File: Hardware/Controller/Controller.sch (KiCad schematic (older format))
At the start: 6 parts

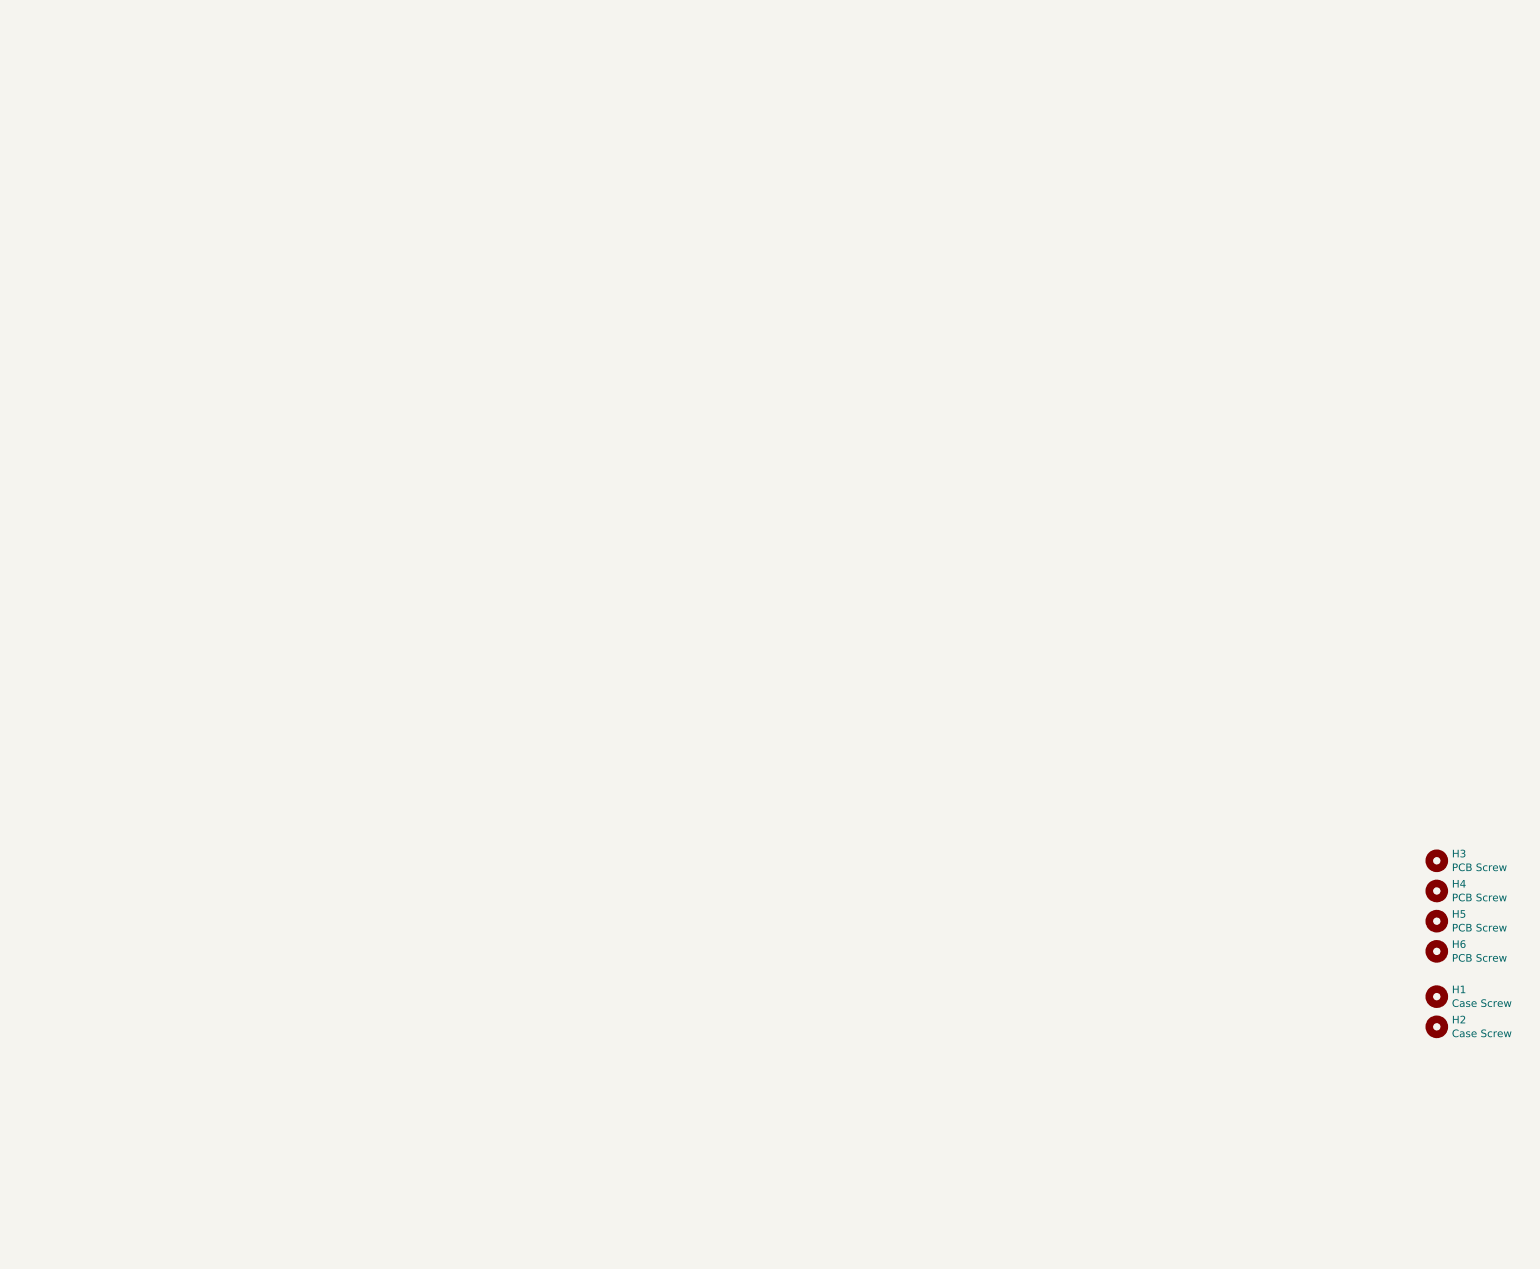
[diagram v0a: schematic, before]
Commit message: Updated fitting for SP 2090 enclosure
Better fit, but still not perfect.
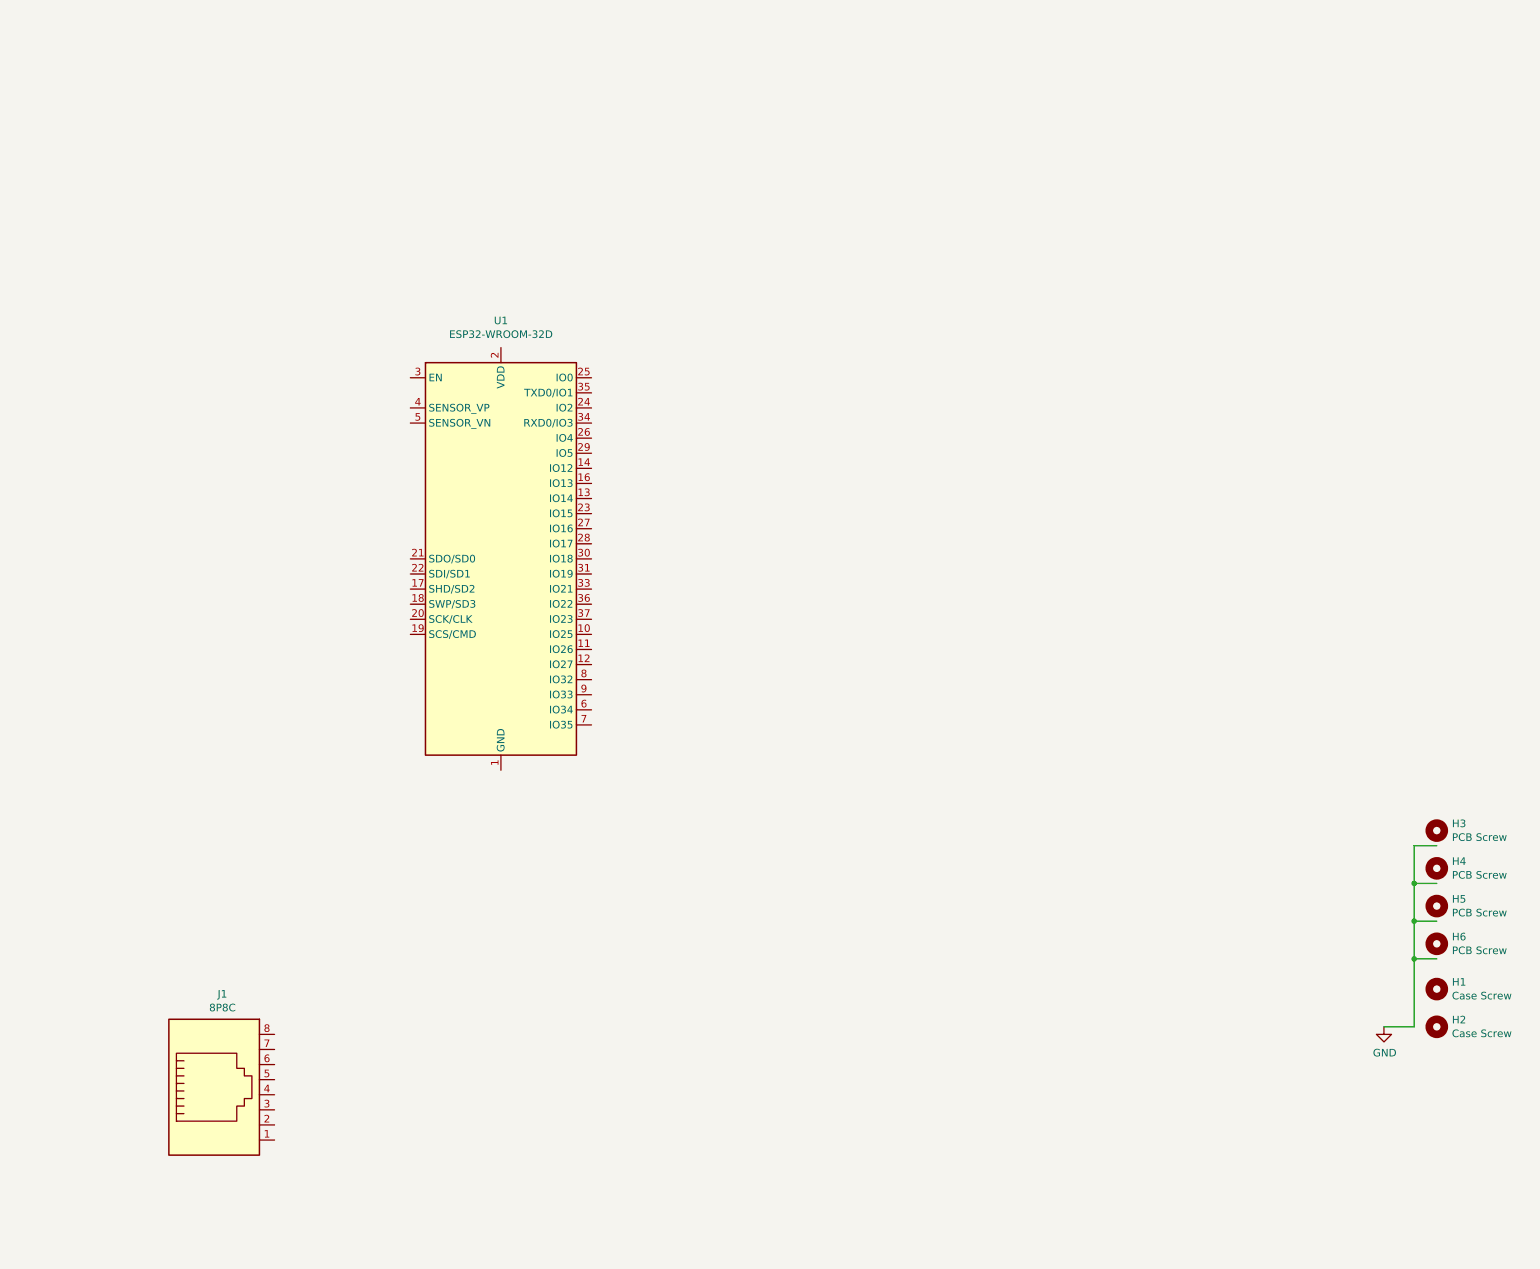
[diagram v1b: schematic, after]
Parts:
- added J1: 8P8C, Connector_RJ:RJ45_Amphenol_54602-x08_Horizontal, symbol Connector:8P8C
- added U1: ESP32-WROOM-32D, RF_Module:ESP32-WROOM-32, symbol RF_Module:ESP32-WROOM-32D
- H3, H4, H5, H6: footprint MountingHole:MountingHole_2.5mm -> MountingHole:MountingHole_2.7mm_M2.5
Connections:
- net labels added: GND
- wire segments 0 -> 9
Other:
- moved on the sheet: H1, H3, H4, H5, H6
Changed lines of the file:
@@
 EESchema Schematic File Version 4
+LIBS:Controller-cache
 EELAYER 26 0
 EELAYER END
@@
 L Mechanical:MountingHole H1
 U 1 1 5C67C5A6
-P 10000 6100
-F 0 "H1" H 10100 6146 50  0000 L CNN
-F 1 "Case Screw" H 10100 6055 50  0000 L CNN
-F 2 "MountingHole:MountingHole_5.3mm_M5" H 10000 6100 50  0001 C CNN
-F 3 "~" H 10000 6100 50  0001 C CNN
-	1    10000 6100
+P 10000 6050
+F 0 "H1" H 10100 6096 50  0000 L CNN
+F 1 "Case Screw" H 10100 6005 50  0000 L CNN
+F 2 "MountingHole:MountingHole_5.3mm_M5" H 10000 6050 50  0001 C CNN
+F 3 "~" H 10000 6050 50  0001 C CNN
+	1    10000 6050
 	1    0    0    -1
 $EndComp
@@
 L Mechanical:MountingHole H6
 U 1 1 5C67C6B3
-P 10000 5800
-F 0 "H6" H 10100 5846 50  0000 L CNN
-F 1 "PCB Screw" H 10100 5755 50  0000 L CNN
-F 2 "MountingHole:MountingHole_2.5mm" H 10000 5800 50  0001 C CNN
-F 3 "~" H 10000 5800 50  0001 C CNN
-	1    10000 5800
+P 10000 5750
+F 0 "H6" H 10100 5796 50  0000 L CNN
+F 1 "PCB Screw" H 10100 5705 50  0000 L CNN
+F 2 "MountingHole:MountingHole_2.7mm_M2.5" H 10000 5750 50  0001 C CNN
+F 3 "~" H 10000 5750 50  0001 C CNN
+	1    10000 5750
 	1    0    0    -1
 $EndComp
@@
 L Mechanical:MountingHole H5
 U 1 1 5C67C6E9
-P 10000 5600
-F 0 "H5" H 10100 5646 50  0000 L CNN
-F 1 "PCB Screw" H 10100 5555 50  0000 L CNN
-F 2 "MountingHole:MountingHole_2.5mm" H 10000 5600 50  0001 C CNN
-F 3 "~" H 10000 5600 50  0001 C CNN
-	1    10000 5600
+P 10000 5500
+F 0 "H5" H 10100 5546 50  0000 L CNN
+F 1 "PCB Screw" H 10100 5455 50  0000 L CNN
+F 2 "MountingHole:MountingHole_2.7mm_M2.5" H 10000 5500 50  0001 C CNN
+F 3 "~" H 10000 5500 50  0001 C CNN
+	1    10000 5500
 	1    0    0    -1
 $EndComp
@@
 L Mechanical:MountingHole H4
 U 1 1 5C67C721
-P 10000 5400
-F 0 "H4" H 10100 5446 50  0000 L CNN
-F 1 "PCB Screw" H 10100 5355 50  0000 L CNN
-F 2 "MountingHole:MountingHole_2.5mm" H 10000 5400 50  0001 C CNN
-F 3 "~" H 10000 5400 50  0001 C CNN
-	1    10000 5400
+P 10000 5250
+F 0 "H4" H 10100 5296 50  0000 L CNN
+F 1 "PCB Screw" H 10100 5205 50  0000 L CNN
+F 2 "MountingHole:MountingHole_2.7mm_M2.5" H 10000 5250 50  0001 C CNN
+F 3 "~" H 10000 5250 50  0001 C CNN
+	1    10000 5250
 	1    0    0    -1
 $EndComp
@@
 L Mechanical:MountingHole H3
 U 1 1 5C67C753
-P 10000 5200
-F 0 "H3" H 10100 5246 50  0000 L CNN
-F 1 "PCB Screw" H 10100 5155 50  0000 L CNN
-F 2 "MountingHole:MountingHole_2.5mm" H 10000 5200 50  0001 C CNN
-F 3 "~" H 10000 5200 50  0001 C CNN
-	1    10000 5200
+P 10000 5000
+F 0 "H3" H 10100 5046 50  0000 L CNN
+F 1 "PCB Screw" H 10100 4955 50  0000 L CNN
+F 2 "MountingHole:MountingHole_2.7mm_M2.5" H 10000 5000 50  0001 C CNN
+F 3 "~" H 10000 5000 50  0001 C CNN
+	1    10000 5000
 	1    0    0    -1
 $EndComp
+$Comp
+L power:GND #PWR0101
+U 1 1 5C688870
+P 9650 6300
+F 0 "#PWR0101" H 9650 6050 50  0001 C CNN
+F 1 "GND" H 9655 6127 50  0000 C CNN
+F 2 "" H 9650 6300 50  0001 C CNN
+F 3 "" H 9650 6300 50  0001 C CNN
+	1    9650 6300
+	1    0    0    -1
+$EndComp
+Wire Wire Line
+	10000 5100 9850 5100
+Wire Wire Line
+	9850 5100 9850 5350
+Wire Wire Line
+	9850 6300 9650 6300
+Wire Wire Line
+	10000 5850 9850 5850
+Connection ~ 9850 5850
+Wire Wire Line
+	10000 5600 9850 5600
+Connection ~ 9850 5600
+Wire Wire Line
+	9850 5600 9850 5850
+Wire Wire Line
+	10000 5350 9850 5350
+Connection ~ 9850 5350
+Wire Wire Line
+	9850 5350 9850 5600
+Wire Wire Line
+	9850 5850 9850 6300
+$Comp
+L RF_Module:ESP32-WROOM-32D U1
+U 1 1 5C688B86
+P 3800 3200
+F 0 "U1" H 3800 4778 50  0000 C CNN
+F 1 "ESP32-WROOM-32D" H 3800 4687 50  0000 C CNN
+F 2 "RF_Module:ESP32-WROOM-32" H 3800 1700 50  0001 C CNN
+F 3 "https://www.espressif.com/sites/default/files/documentation/esp32-wroom-32d_esp32-wroom-32u_datasheet_en.pdf" H 3500 3250 50  0001 C CNN
+	1    3800 3200
+	1    0    0    -1
+$EndComp
+$Comp
+L Connector:8P8C J1
+U 1 1 5C688D10
+P 1900 6750
+F 0 "J1" H 1955 7417 50  0000 C CNN
+F 1 "8P8C" H 1955 7326 50  0000 C CNN
+F 2 "Connector_RJ:RJ45_Amphenol_54602-x08_Horizontal" V 1900 6775 50  0001 C CNN
+F 3 "~" V 1900 6775 50  0001 C CNN
+	1    1900 6750
+	1    0    0    -1
+$EndComp

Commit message: Added a first set of parts
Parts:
- added J2: LCD Header, Connector_PinHeader_2.54mm:PinHeader_1x04_P2.54mm_Vertical, symbol Connector:Conn_01x04_Female
- added J3: USB_B_Micro, Connector_USB:USB_Micro-B_Amphenol_10103594-0001LF_Horizontal, symbol Connector:USB_B_Micro
- added J4: S88 ShiftRegister, Connector_Molex:Molex_Micro-Latch_53254-0670_1x06_P2.00mm_Horizontal, symbol Connector_Generic:Conn_01x06
- added SW1: Rotary_Encoder_Switch, Rotary_Encoder:RotaryEncoder_Alps_EC11E-Switch_Vertical_H20mm, symbol Device:Rotary_Encoder_Switch
- added SW2, SW3, SW4, SW5, SW6: SW_Push_Dual, Button_Switch_THT:SW_TH_Tactile_Omron_B3F-10xx, symbol Switch:SW_Push_Dual
- added SW7: Shift, Button_Switch_THT:SW_TH_Tactile_Omron_B3F-10xx, symbol Switch:SW_Push_Dual
- added SW8: Stop, Button_Switch_THT:SW_TH_Tactile_Omron_B3F-10xx, symbol Switch:SW_Push_Dual
- added U2: TJA1051T, Package_SO:SOIC-8_3.9x4.9mm_P1.27mm, symbol Interface_CAN_LIN:TJA1051T
- added U3: 74HC36, Package_DIP:DIP-14_W7.62mm_Socket, symbol 74xx_IEEE:74HC36
- H3, H4, H5, H6: symbol Mechanical:MountingHole -> Mechanical:MountingHole_Pad
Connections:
- net labels added: VCC
- wire segments 9 -> 42

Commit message: Added more parts
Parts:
- removed U3: 74HC36, Package_DIP:DIP-14_W7.62mm_Socket, symbol 74xx_IEEE:74HC36
- added C1, C10, C2, C3, C4, C5, C6, C7, C8, C9: 10n, Capacitor_SMD:C_0805_2012Metric_Pad1.15x1.40mm_HandSolder, symbol Device:C
- added R1, R10, R11, R12, R13, R14, R15, R16, R17, R18, R19, R2, R20, R3, R4, R5, R6, R7, R8, R9: 10k, Resistor_SMD:R_0603_1608Metric_Pad1.05x0.95mm_HandSolder, symbol Device:R
- added U3: 74LS367, Package_SO:SOP-16_4.4x10.4mm_P1.27mm, symbol 74xx:74LS367
- added U4: CH340C, Package_SO:SOIC-16_3.9x9.9mm_P1.27mm, symbol Interface_USB:CH340G
- U1: value ESP32-WROOM-32D -> ESP32-WROOM-32; symbol RF_Module:ESP32-WROOM-32D -> RF_Module:ESP32-WROOM-32
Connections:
- net GND: now also J1.5, J1.6, J2.1 (Pin_1), J4.2 (Pin_2), U2.2 (GND), C1.1, C10.1, C2.1, C3.1, C4.1, C5.1, C6.1, C7.1, C8.1, C9.1, U3.1 (OEa), U3.10 (I4), U3.12 (I5), U3.14 (I6), U3.8 (GND), U4.1 (GND)
- net VCC: now also J2.2 (Pin_2), J4.6 (Pin_6), U2.3 (VCC), R1.2, R11.2, R13.2, R15.2, R17.2, R19.1, R3.2, R5.2, R7.2, R9.2, U3.15 (OEb), U3.16 (VCC), U4.16 (VCC), U4.4 (V3)
- net I2C_SCL: now reaches U1.11 (IO26)
- net I2C_SCL: now also J2.3 (Pin_3)
- net I2C_SDA: now reaches U1.12 (IO27)
- net I2C_SDA: now also J2.4 (Pin_4)
- net at U1.13 (IO14): now also C5.2, R10.2
- net at U1.14 (IO12): now also C3.2, R6.2
- net at U1.16 (IO13): now also C4.2, R8.2
- net at U1.23 (IO15): now also C6.2, R12.2
- net at U1.25 (IO0): now also U4.13 (~DTR)
- net at U1.26 (IO4): now also U2.4 (RXD)
- net at U1.27 (IO16): now also C7.2, R14.2
- net at U1.28 (IO17): now also C8.2, R16.2
- net at U1.29 (IO5): now also U2.1 (TXD)
- net at U1.3 (EN): now also U4.14 (~RTS)
- net at U1.31 (IO19): now also C9.2, R18.2
- net at U1.34 (RXD0/IO3): now also U4.3 (RXD)
- net at U1.35 (TXD0/IO1): now also U4.2 (TXD)
- net S88_CLOCK_UC: now reaches U1.6 (IO34)
- net S88_CLOCK_UC: now also U3.6 (I3)
- net S88_PS_UC: now reaches U1.7 (IO35)
- net S88_PS_UC: now also U3.4 (I2)
- net S88_RESET_UC: now reaches U1.8 (IO32)
- net S88_RESET_UC: now also U3.2 (I1)
- net S88_DATA: now reaches U1.9 (IO33)
- net S88_DATA: now also J4.1 (Pin_1)
- net at J1.1: now also U2.7 (CANH)
- net at J1.2: now also U2.6 (CANL)
- net at SW1.A: now also R1.1, R2.1
- net at SW1.B: now also R3.1, R4.1
- net at SW1.S1: now also R19.2, R20.2
- net at SW2.1, SW2.3: now also R5.1, R6.1
- net at SW3.1, SW3.3: now also R7.1, R8.1
- net at SW4.1, SW4.3: now also R10.1, R9.1
- net at SW5.1, SW5.3: now also R11.1, R12.1
- net at SW6.1, SW6.3: now also R13.1, R14.1
- net at SW7.1, SW7.3: now also R15.1, R16.1
- net at SW8.1, SW8.3: now also R17.1, R18.1
- net at J3.2 (D-): now also U4.6 (UD-)
- net at J3.3 (D+): now also U4.5 (UD+)
- net at J4.3 (Pin_3): now also U3.7 (O3a)
- net at J4.4 (Pin_4): now also U3.5 (O2a)
- net at J4.5 (Pin_5): now also U3.3 (O1a)
- new net: C1.2, R2.2
- new net: C2.2, R4.2
- new net: C10.2, R20.1
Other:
- moved on the sheet: J1, J2, J3, J4, SW1, SW2, SW3, SW4, SW5, SW6, SW7, SW8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

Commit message: Added XM1548 and worked on Hardware
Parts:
- added C11: 100n, Capacitor_SMD:C_0805_2012Metric_Pad1.15x1.40mm_HandSolder, symbol Device:C
- added C12: 470u, Capacitor_THT:CP_Radial_D6.3mm_P2.50mm, symbol Device:CP
- added C13: 4u7, Capacitor_THT:CP_Radial_D6.3mm_P2.50mm, symbol Device:CP
- added D1, D2, D3: D_Schottky, Diode_SMD:D_0603_1608Metric_Pad1.05x0.95mm_HandSolder, symbol Device:D_Schottky
- added J5: Screw_Terminal_01x05, TerminalBlock_RND:TerminalBlock_RND_205-00015_1x05_P5.00mm_Horizontal, symbol Connector:Screw_Terminal_01x05
- added U5: XM1584, Controller:XM1584, symbol ControllerParts:XM1584
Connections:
- net GND: now also C11.2, C12.2, C13.2, J5.2 (Pin_2), U5.1 (In-), U5.2 (In-), U5.5 (Out-), U5.6 (Out-)
- net VCC: now also C12.1, C13.1, J5.1 (Pin_1), U5.7 (Out+), U5.8 (Out+)
- net at U1.3 (EN), U4.14 (~RTS): now also C11.1
- net at U1.30 (IO18): now also C1.2, R2.2
- net at U1.33 (IO21): now also C2.2, R4.2
- net at U1.36 (IO22): now also C10.2, R20.1
- net CANH: now reaches J1.1, U2.7 (CANH)
- net CANH: now also J5.5 (Pin_5)
- net CANL: now reaches J1.2, U2.6 (CANL)
- net CANL: now also J5.4 (Pin_4)
- net at J1.3: now also J1.4, D1.2 (A)
- net at J3.1 (VBUS): now also D2.2 (A)
- new net: D3.2 (A), J5.3 (Pin_3)
- new net: D1.1 (K), D2.1 (K), D3.1 (K), U5.3 (In+), U5.4 (In+)
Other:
- moved on the sheet: J2, U2, U4
